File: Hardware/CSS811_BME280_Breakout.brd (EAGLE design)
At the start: 38.1 x 38.1 mm, 31 parts, among them J1 GATORGATOR_MINI, J2 GATORGATOR_MINI, J3 GATORGATOR_MINI, J4 GATORGATOR_MINI, J5 GATORGATOR_MINI, J6 GATORGATOR_MINI, J7 GATORGATOR_MINI, J8 GATORGATOR_MINI, U2 CCS811, U3 BME280

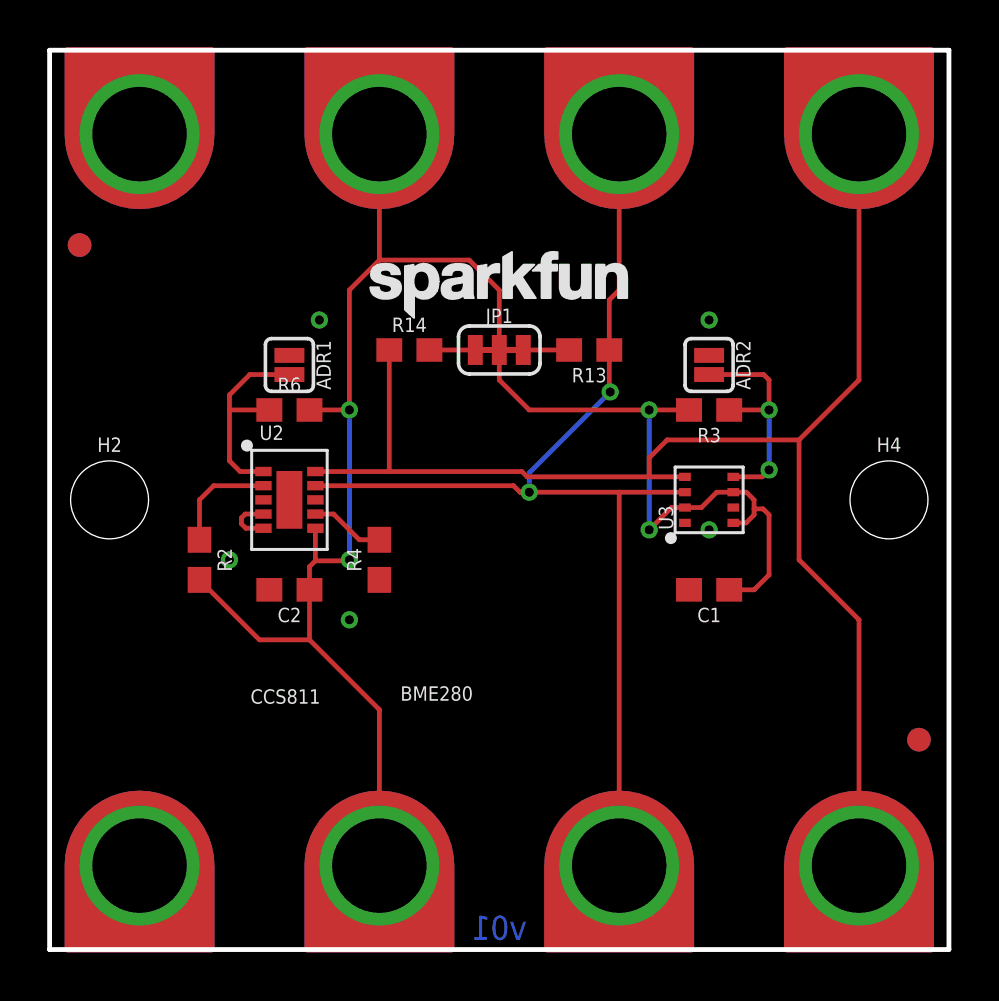
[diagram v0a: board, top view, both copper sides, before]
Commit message: resizing board, adding silk
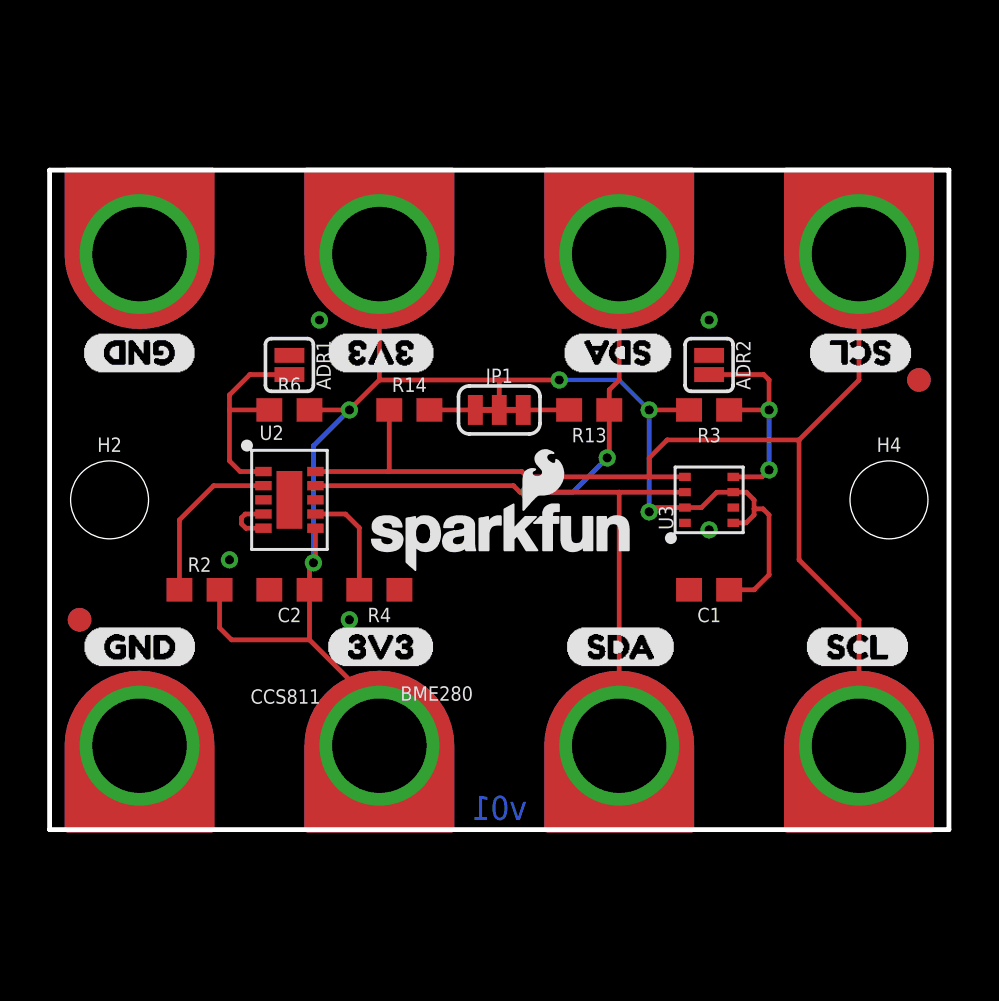
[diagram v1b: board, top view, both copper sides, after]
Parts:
- removed LOGO3: SFE_LOGO_NAME.1_INCH, SparkFun-Aesthetics:SFE_LOGO_NAME_.1
- added LOGO2: SFE_LOGO_NAME_FLAME.1_INCH, SparkFun-Aesthetics:SFE_LOGO_NAME_FLAME_.1
- added U$1, U$16, U$8, U$9: (no value), buzzard_labels:3V33
- added U$10, U$15, U$2, U$7: (no value), buzzard_labels:GND0
- added U$11, U$14, U$3, U$6: (no value), buzzard_labels:SCL2
- added U$12, U$13, U$4, U$5: (no value), buzzard_labels:SDA1
- LOGO1: value SFE_LOGO_NAME.1_INCH -> SFE_LOGO_NAME_FLAME.1_INCH; device SparkFun-Aesthetics:SFE_LOGO_NAME_.1 -> SparkFun-Aesthetics:SFE_LOGO_NAME_FLAME_.1
- moved FD1 36.0 mm to (36.8, 24.1)
- moved FD4 36.0 mm to (36.8, 24.1)
- moved FD2 35.9 mm to (1.27, 14.0)
- moved FD3 35.9 mm to (1.27, 14.0)
- moved LOGO1 10.7 mm to (19.2, 17.5)
- moved J1 5.08 mm to (34.3, 8.89)
- moved J2 5.08 mm to (24.1, 8.89)
- moved J3 5.08 mm to (14.0, 8.89)
- moved J4 5.08 mm to (3.81, 8.89)
- moved LOGO4 5.08 mm to (19.1, 6.35)
- moved J5 5.08 mm to (3.81, 29.2)
- moved J6 5.08 mm to (14.0, 29.2)
- moved J7 5.08 mm to (24.1, 29.2)
- moved J8 5.08 mm to (34.3, 29.2)
- moved JP1 2.54 mm to (19.1, 22.9)
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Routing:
- net 3.3V: track 78.2 -> 63.2 mm, vias 4 -> 5
- net SCL: track 61.5 -> 48.8 mm
- net SDA: track 48.4 -> 39.3 mm
- net !RST: track 4.65 -> 7.12 mm
- net !WAKE: track 3.16 -> 4.73 mm
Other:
- board size 38.1 x 38.1 mm -> 38.1 x 27.9 mm
- board text removed: "Nathan Seidle"

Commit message: finalizing layout/silk
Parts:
- removed ADR1, ADR2: (no value), SparkFun-Jumpers:SMT-JUMPER_2_NO_SILK
- removed JP1: (no value), SparkFun-Jumpers:SMT-JUMPER_3_2-NC_TRACE_SILK
- LOGO1: value SFE_LOGO_NAME_FLAME.1_INCH -> SFE_LOGO_NAME.1_INCH; device SparkFun-Aesthetics:SFE_LOGO_NAME_FLAME_.1 -> SparkFun-Aesthetics:SFE_LOGO_NAME_.1
- R13, R14: value 4.7k -> 10k
- moved R14 2.62 mm to (17.8, 22.2), turned to 90 degrees
- moved R13 2.62 mm to (20.3, 22.2), turned to 90 degrees
- moved U$10 2.54 mm to (1.40, 27.8)
- moved U$11 2.54 mm to (32.0, 27.8)
- moved U$12 2.54 mm to (21.8, 27.8)
- moved U$9 2.54 mm to (11.7, 27.8)
- moved J5 2.54 mm to (3.81, 26.7)
- moved J6 2.54 mm to (14.0, 26.7)
- moved J7 2.54 mm to (24.1, 26.7)
- moved J8 2.54 mm to (34.3, 26.7)
- moved U$5 2.54 mm to (26.4, 22.7)
- moved U$6 2.54 mm to (36.6, 22.7)
- moved U$7 2.54 mm to (6.22, 22.7)
- moved U$8 2.54 mm to (16.4, 22.7)
- moved H2 1.27 mm to (2.54, 17.8)
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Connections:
- removed net N$4: JP1.3, R13.2
- removed net N$5: JP1.1, R14.2
- net 3.3V: now also R13.2, R14.2; no longer JP1.2
- net CCS811_ADDR: no longer ADR1.2
- net GND: no longer ADR1.1, ADR2.1
- net SDO/ADR: no longer ADR2.2
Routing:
- net SCL: track 48.8 -> 44.7 mm
- net SDO/ADR: track 9.77 -> 5.87 mm
- net CCS811_ADDR: track 9.01 -> 5.18 mm
- net SDA: track 39.3 -> 36.8 mm
- net N$4: track 1.94 -> 0.00 mm
- net N$5: track 1.94 -> 0.00 mm
- net 3.3V: track 63.2 -> 64.0 mm
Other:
- board size 38.1 x 27.9 mm -> 38.1 x 25.4 mm
- board text removed: "Measurements in mm"

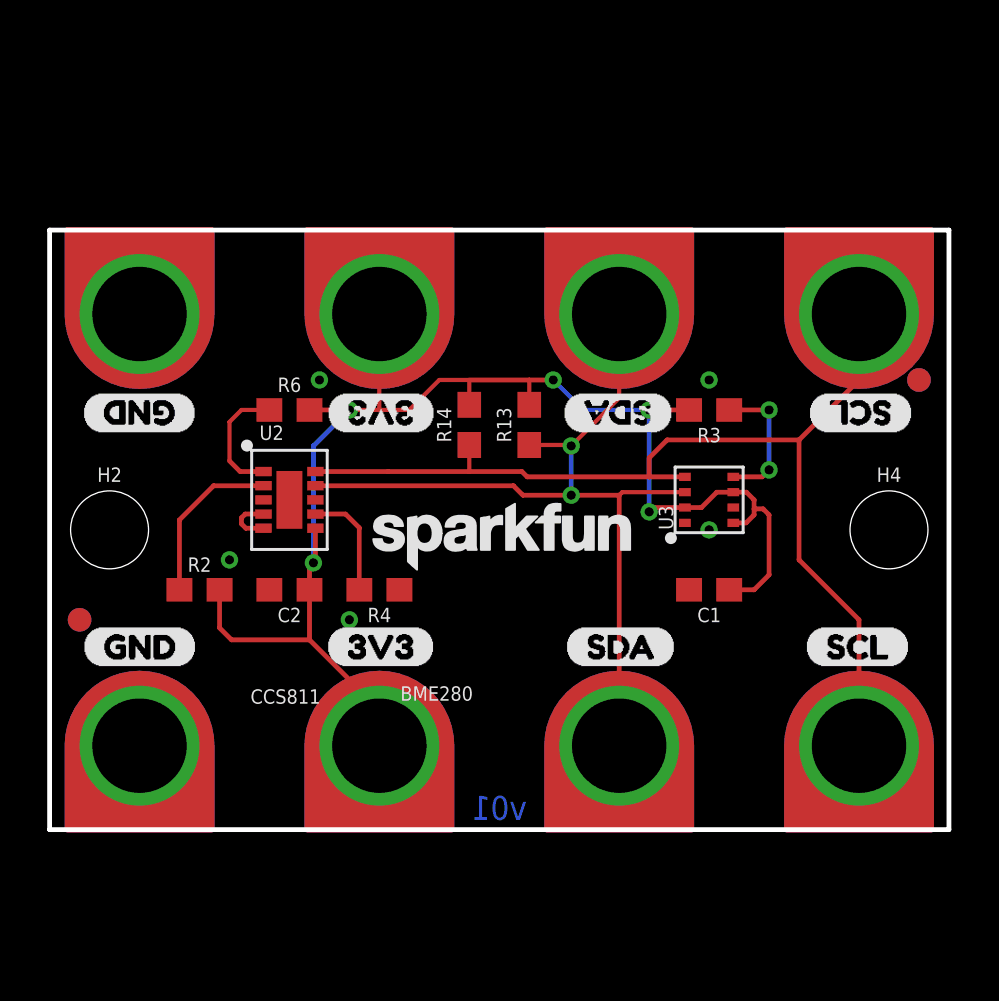
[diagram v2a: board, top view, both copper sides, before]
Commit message: adding protection diodes
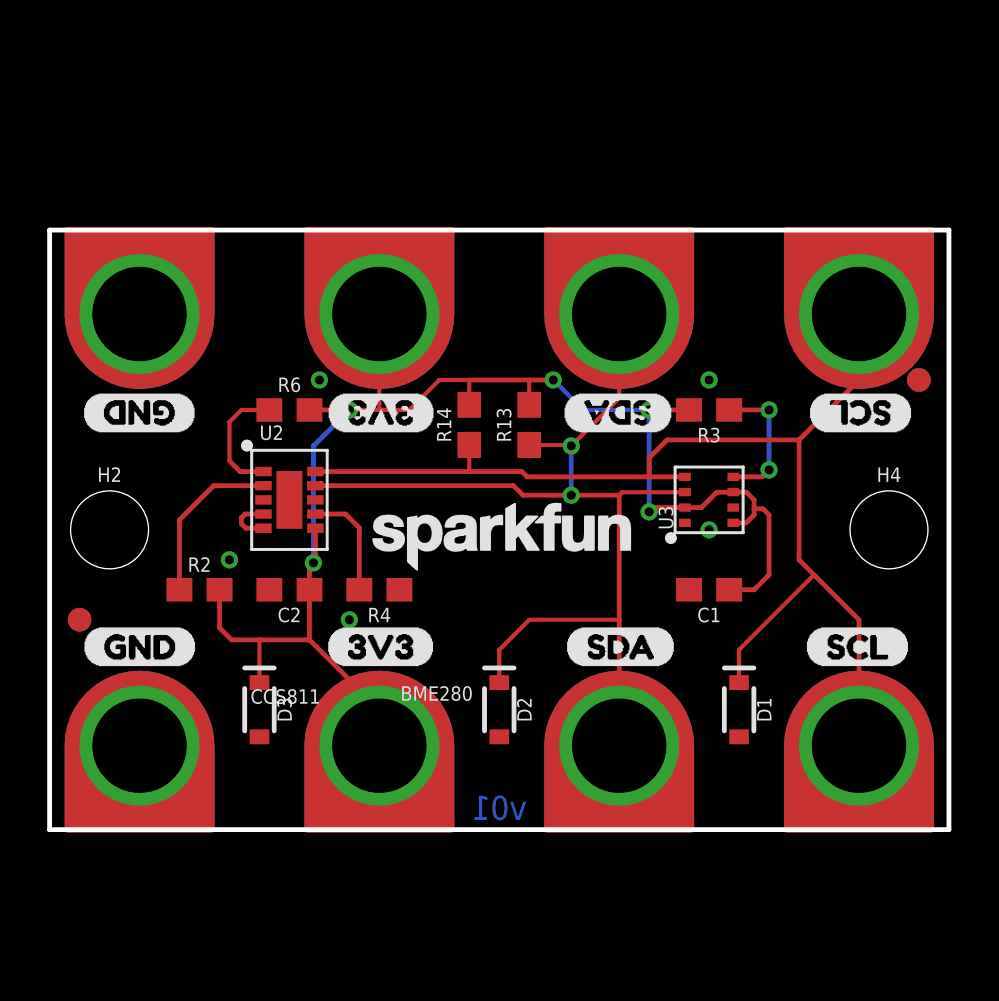
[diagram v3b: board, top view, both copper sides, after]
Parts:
- added D1, D2, D3: 3.6V, SparkFun-DiscreteSemi:SOD-323
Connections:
- net 3.3V: now also D3.C
- net GND: now also D1.A, D2.A, D3.A
- net SCL: now also D1.C
- net SDA: now also D2.C
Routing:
- net SDA: track 36.8 -> 43.8 mm
- net SCL: track 44.7 -> 50.6 mm
- net 3.3V: track 64.0 -> 65.8 mm
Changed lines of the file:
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@@
 <?xml version="1.0" encoding="utf-8"?>
 <!DOCTYPE eagle SYSTEM "eagle.dtd">
-<eagle version="9.1.0">
+<eagle version="9.3.1">
 <drawing>
 <settings>
@@
 <element name="U$16" library="buzzard_labels" package="3V33" value="" x="16.383" y="12.827" smashed="yes" rot="MR0"/>
 <element name="LOGO2" library="SparkFun-Aesthetics" package="SFE_LOGO_NAME_FLAME_.1" value="SFE_LOGO_NAME_FLAME.1_INCH" x="19.05" y="17.526" smashed="yes" rot="MR0"/>
+<element name="D1" library="SparkFun-DiscreteSemi" package="SOD-323" value="3.6V" x="29.21" y="10.16" smashed="yes" rot="R270">
+<attribute name="NAME" x="29.972" y="10.16" size="0.6096" layer="25" font="vector" ratio="20" rot="R270" align="bottom-center"/>
+<attribute name="PROD_ID" value="DIO-08199" x="29.21" y="10.16" size="1.778" layer="27" rot="R270" display="off"/>
+<attribute name="VALUE" x="28.448" y="10.16" size="0.6096" layer="27" font="vector" ratio="20" rot="R270" align="top-center"/>
+</element>
+<element name="D2" library="SparkFun-DiscreteSemi" package="SOD-323" value="3.6V" x="19.05" y="10.16" smashed="yes" rot="R270">
+<attribute name="NAME" x="19.812" y="10.16" size="0.6096" layer="25" font="vector" ratio="20" rot="R270" align="bottom-center"/>
+<attribute name="PROD_ID" value="DIO-08199" x="19.05" y="10.16" size="1.778" layer="27" rot="R270" display="off"/>
+<attribute name="VALUE" x="18.288" y="10.16" size="0.6096" layer="27" font="vector" ratio="20" rot="R270" align="top-center"/>
+</element>
+<element name="D3" library="SparkFun-DiscreteSemi" package="SOD-323" value="3.6V" x="8.89" y="10.16" smashed="yes" rot="R270">
+<attribute name="NAME" x="9.652" y="10.16" size="0.6096" layer="25" font="vector" ratio="20" rot="R270" align="bottom-center"/>
+<attribute name="PROD_ID" value="DIO-08199" x="8.89" y="10.16" size="1.778" layer="27" rot="R270" display="off"/>
+<attribute name="VALUE" x="8.128" y="10.16" size="0.6096" layer="27" font="vector" ratio="20" rot="R270" align="top-center"/>
+</element>
 </elements>
 <signals>
@@
 <via x="7.62" y="16.51" extent="1-16" drill="0.381"/>
 <via x="12.7" y="13.97" extent="1-16" drill="0.381"/>
+<contactref element="D3" pad="A"/>
+<contactref element="D2" pad="A"/>
+<contactref element="D1" pad="A"/>
 </signal>
 <signal name="SCL">
@@
 <wire x1="20.234" y1="20.025" x2="20.009" y2="20.25" width="0.2032" layer="1"/>
 <wire x1="20.009" y1="20.25" x2="17.78" y2="20.25" width="0.2032" layer="1"/>
-<wire x1="17.78" y1="20.25" x2="14.351" y2="20.25" width="0.2032" layer="1"/>
-<wire x1="14.351" y1="20.25" x2="11.26" y2="20.25" width="0.2032" layer="1"/>
+<wire x1="17.78" y1="20.25" x2="11.26" y2="20.25" width="0.2032" layer="1"/>
 <wire x1="34.29" y1="26.924" x2="34.29" y2="24.13" width="0.2032" layer="1"/>
 <wire x1="31.75" y1="21.59" x2="31.75" y2="16.51" width="0.2032" layer="1"/>
-<wire x1="31.75" y1="16.51" x2="34.29" y2="13.97" width="0.2032" layer="1"/>
+<wire x1="31.75" y1="16.51" x2="32.385" y2="15.875" width="0.2032" layer="1"/>
+<wire x1="32.385" y1="15.875" x2="34.29" y2="13.97" width="0.2032" layer="1"/>
 <wire x1="34.29" y1="24.13" x2="31.75" y2="21.59" width="0.2032" layer="1"/>
 <wire x1="34.29" y1="13.97" x2="34.29" y2="8.636" width="0.2032" layer="1"/>
@@
 <wire x1="26.162" y1="21.59" x2="31.75" y2="21.59" width="0.2032" layer="1"/>
 <wire x1="17.78" y1="21.375" x2="17.78" y2="20.25" width="0.1778" layer="1"/>
+<contactref element="D1" pad="C"/>
+<wire x1="29.21" y1="11.31" x2="29.21" y2="12.7" width="0.1778" layer="1"/>
+<wire x1="29.21" y1="12.7" x2="32.385" y2="15.875" width="0.1778" layer="1"/>
 </signal>
 <signal name="SDA">
@@
 <via x="22.098" y="19.248" extent="1-16" drill="0.381"/>
 <wire x1="24.13" y1="24.13" x2="24.13" y2="26.924" width="0.2032" layer="1"/>
-<wire x1="24.13" y1="8.636" x2="24.13" y2="19.248" width="0.2032" layer="1"/>
+<wire x1="24.13" y1="8.636" x2="24.13" y2="13.97" width="0.2032" layer="1"/>
+<wire x1="24.13" y1="13.97" x2="24.13" y2="19.248" width="0.2032" layer="1"/>
 <wire x1="20.32" y1="21.375" x2="22.059" y2="21.375" width="0.1778" layer="1"/>
 <wire x1="22.059" y1="21.375" x2="22.098" y2="21.336" width="0.1778" layer="1"/>
@@
 <wire x1="24.13" y1="19.248" x2="24.257" y2="19.375" width="0.1778" layer="1"/>
 <wire x1="24.257" y1="19.375" x2="26.915" y2="19.375" width="0.1778" layer="1"/>
+<contactref element="D2" pad="C"/>
+<wire x1="19.05" y1="11.31" x2="19.05" y2="12.7" width="0.1778" layer="1"/>
+<wire x1="19.05" y1="12.7" x2="20.32" y2="13.97" width="0.1778" layer="1"/>
+<wire x1="20.32" y1="13.97" x2="24.13" y2="13.97" width="0.1778" layer="1"/>
 </signal>
 <signal name="3.3V">
@@
 <wire x1="7.2" y1="15.24" x2="7.2" y2="13.628" width="0.2032" layer="1"/>
 <wire x1="7.2" y1="13.628" x2="7.708" y2="13.12" width="0.2032" layer="1"/>
-<wire x1="7.708" y1="13.12" x2="11.01" y2="13.12" width="0.2032" layer="1"/>
+<wire x1="7.708" y1="13.12" x2="8.89" y2="13.12" width="0.2032" layer="1"/>
+<wire x1="8.89" y1="13.12" x2="11.01" y2="13.12" width="0.2032" layer="1"/>
 <wire x1="11.01" y1="13.12" x2="13.97" y2="10.16" width="0.2032" layer="1"/>
 <wire x1="13.97" y1="10.16" x2="13.97" y2="8.636" width="0.2032" layer="1"/>
@@
 <wire x1="13.97" y1="22.86" x2="15.24" y2="22.86" width="0.1778" layer="1"/>
 <wire x1="13.97" y1="22.86" x2="13.97" y2="25.4" width="0.1778" layer="1"/>
+<contactref element="D3" pad="C"/>
+<wire x1="8.89" y1="11.31" x2="8.89" y2="13.12" width="0.1778" layer="1"/>
 </signal>
 <signal name="!RST">

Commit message: finalizing silk
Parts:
- added U$17: (no value), buzzard_labels (4):GATOR#AIR0
- added U$18: (no value), GatorBit_Final_for_Silk#01#png (2):GATORBIT_FINAL_FOR_SILK#01#PNG
- added U$19: (no value), GatorBit_Final_for_Silk#01#png (3):GATORBIT_FINAL_FOR_SILK#01#PNG
- moved FD1 2.54 mm to (36.8, 21.6)
- moved FD4 2.54 mm to (36.8, 21.6)
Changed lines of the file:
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@@
 <?xml version="1.0" encoding="utf-8"?>
 <!DOCTYPE eagle SYSTEM "eagle.dtd">
-<eagle version="9.3.1">
+<eagle version="9.1.0">
 <drawing>
 <settings>
@@
 <setting verticaltext="up"/>
 </settings>
-<grid distance="0.05" unitdist="inch" unit="inch" style="lines" multiple="1" display="yes" altdistance="0.005" altunitdist="inch" altunit="inch"/>
+<grid distance="0.05" unitdist="inch" unit="mm" style="lines" multiple="1" display="yes" altdistance="0.005" altunitdist="inch" altunit="inch"/>
 <layers>
 <layer number="1" name="Top" color="4" fill="1" visible="yes" active="yes"/>
@@
 </element>
 <element name="LOGO4" library="SparkFun-Aesthetics" package="OSHW-LOGO-S" value="OSHW-LOGOS" x="19.05" y="6.35" smashed="yes" rot="MR0"/>
-<element name="FD1" library="SparkFun-Aesthetics" package="FIDUCIAL-1X2" value="FIDUCIAL1X2" x="36.83" y="24.13" smashed="yes"/>
+<element name="FD1" library="SparkFun-Aesthetics" package="FIDUCIAL-1X2" value="FIDUCIAL1X2" x="36.83" y="21.59" smashed="yes"/>
 <element name="FD2" library="SparkFun-Aesthetics" package="FIDUCIAL-1X2" value="FIDUCIAL1X2" x="1.27" y="13.97" smashed="yes"/>
 <element name="R2" library="SparkFun-Resistors" package="0603" value="4.7k" x="6.35" y="15.24" smashed="yes">
@@
 <element name="LOGO1" library="SparkFun-Aesthetics" package="SFE_LOGO_NAME_.1" value="SFE_LOGO_NAME.1_INCH" x="19.177" y="17.49425" smashed="yes"/>
 <element name="FD3" library="SparkFun-Aesthetics" package="FIDUCIAL-1X2" value="FIDUCIAL1X2" x="1.27" y="13.97" smashed="yes" rot="MR0"/>
-<element name="FD4" library="SparkFun-Aesthetics" package="FIDUCIAL-1X2" value="FIDUCIAL1X2" x="36.83" y="24.13" smashed="yes" rot="MR0"/>
+<element name="FD4" library="SparkFun-Aesthetics" package="FIDUCIAL-1X2" value="FIDUCIAL1X2" x="36.83" y="21.59" smashed="yes" rot="MR0"/>
 <element name="J1" library="SparkFun-Connectors" package="GATOR_MINI" value="GATORGATOR_MINI" x="34.29" y="8.89" smashed="yes"/>
 <element name="J2" library="SparkFun-Connectors" package="GATOR_MINI" value="GATORGATOR_MINI" x="24.13" y="8.89" smashed="yes"/>
@@
 <attribute name="VALUE" x="8.128" y="10.16" size="0.6096" layer="27" font="vector" ratio="20" rot="R270" align="top-center"/>
 </element>
+<element name="U$17" library="buzzard_labels (4)" package="GATOR#AIR0" value="" x="26.035" y="15.367" rot="MR0"/>
+<element name="U$19" library="GatorBit_Final_for_Silk#01#png (3)" package="GATORBIT_FINAL_FOR_SILK#01#PNG" value="" x="18.669" y="12.7" rot="MR0"/>
+<element name="U$18" library="GatorBit_Final_for_Silk#01#png (2)" package="GATORBIT_FINAL_FOR_SILK#01#PNG" value="" x="19.05" y="15.24"/>
 </elements>
 <signals>

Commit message: engineer run of checklist, post review
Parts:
- added D4: RED, SparkFun-LED:LED-0603
- added Q1: 2.5A/30V/105mΩ, SparkFun-DiscreteSemi:SOT23-3
- added R1: 1k, SparkFun-Resistors:0603
- added R5: 10k, SparkFun-Resistors:0603
- added U$20: (no value), buzzard_labels:GND0
- added U$21: (no value), buzzard_labels:3V33
- added U$22: (no value), buzzard_labels:SDA1
- added U$23: (no value), buzzard_labels:SCL2
- U$18: device GatorBit_Final_for_Silk#01#png (2):GATORBIT_FINAL_FOR_SILK#01#PNG -> buzzard_labels (5):PWR0
- moved U$18 3.41 mm to (16.6, 12.8)
- moved D3 2.82 mm to (7.24, 12.4)
- moved U$19 2.54 mm to (18.7, 15.2)
- moved LOGO2 2.54 mm to (19.1, 20.1)
- moved U$17 2.54 mm to (26.0, 17.9)
- moved D1 1.27 mm to (29.2, 8.89)
- moved D2 1.27 mm to (19.1, 8.89)
- moved LOGO1 1.27 mm to (19.2, 18.8)
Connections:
- new net N$2: D4.A, R1.1
- new net N$3: D3.C, J3.P$2, J6.P$2, Q1.3
- new net N$4: D3.A, Q1.1, R5.2
- net 3.3V: now also Q1.2, R1.2; no longer D3.C, J3.P$2, J6.P$2
- net GND: now also D4.C, R5.1; no longer D3.A
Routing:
- net N$3: track 0.00 -> 29.5 mm, vias 0 -> 1
- net 3.3V: track 65.8 -> 62.2 mm, vias 5 -> 6
- net N$4: track 0.00 -> 3.42 mm
- net N$2: track 0.00 -> 1.92 mm
- net SCL: track 50.6 -> 51.9 mm
- net SDA: track 43.8 -> 44.5 mm

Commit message: pushing unsaved changes from checklist
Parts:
- added U$24: (no value), SparkFun-Aesthetics:ORDERING_INSTRUCTIONS
- moved H2 5.08 mm to (2.54, 12.7)
- moved H4 5.08 mm to (35.6, 12.7)
- moved J5 5.08 mm to (3.81, 21.6)
- moved J6 5.08 mm to (14.0, 21.6)
- moved J7 5.08 mm to (24.1, 21.6)
- moved J8 5.08 mm to (34.3, 21.6)
- moved R1 5.08 mm to (19.1, 11.4)
- moved R13 5.08 mm to (20.3, 17.1)
- moved R14 5.08 mm to (17.8, 17.1)
- moved U$20 5.08 mm to (1.40, 17.7)
- moved U$21 5.08 mm to (11.7, 17.7)
- moved U$22 5.08 mm to (21.7, 17.7)
- moved U$23 5.08 mm to (32.1, 17.7)
- moved U$5 5.08 mm to (26.4, 17.7)
- moved U$6 5.08 mm to (36.6, 17.7)
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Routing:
- net !RST: track 7.12 -> 3.79 mm
- net 3.3V: track 62.2 -> 60.3 mm
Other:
- board text added: "Black Gloss Soldermask"
